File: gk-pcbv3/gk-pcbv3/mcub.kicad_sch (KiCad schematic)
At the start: 10 parts, among them U4 STM32H7S7L8H6H, Y1 24MHz

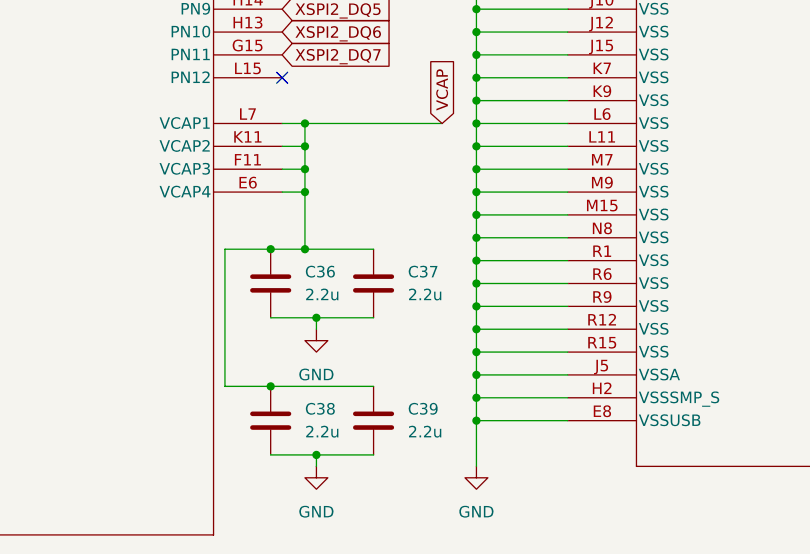
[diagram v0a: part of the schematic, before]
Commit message: redesign for better signal integrity
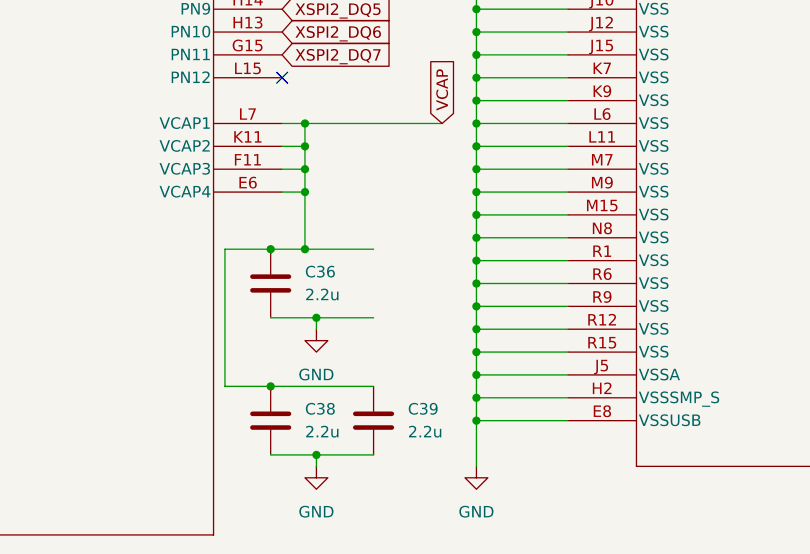
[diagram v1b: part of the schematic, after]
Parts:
- removed C37: 2.2u, Capacitor_SMD:C_0805_2012Metric, symbol Device:C
- C36, C38, C39: footprint Capacitor_SMD:C_0805_2012Metric -> Capacitor_SMD:C_0402_1005Metric
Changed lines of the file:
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@@
 			)
 		)
-		(property "Footprint" "Capacitor_SMD:C_0805_2012Metric"
+		(property "Footprint" "Capacitor_SMD:C_0402_1005Metric"
 			(at 133.0452 151.13 0)
 			(effects
@@
 	)
 	(symbol
-		(lib_id "Device:C")
-		(at 132.08 132.08 0)
-		(unit 1)
-		(exclude_from_sim no)
-		(in_bom yes)
-		(on_board yes)
-		(dnp no)
-		(fields_autoplaced yes)
-		(property "Reference" "C37"
-			(at 135.89 130.8099 0)
-			(effects
-				(font
-					(size 1.27 1.27)
-				)
-				(justify left)
-			)
-		)
-		(property "Value" "2.2u"
-			(at 135.89 133.3499 0)
-			(effects
-				(font
-					(size 1.27 1.27)
-				)
-				(justify left)
-			)
-		)
-		(property "Footprint" "Capacitor_SMD:C_0805_2012Metric"
-			(at 133.0452 135.89 0)
-			(effects
-				(font
-					(size 1.27 1.27)
-				)
-				(hide yes)
-			)
-		)
-		(property "Datasheet" "~"
-			(at 132.08 132.08 0)
-			(effects
-				(font
-					(size 1.27 1.27)
-				)
-				(hide yes)
-			)
-		)
-		(property "Description" "Unpolarized capacitor"
-			(at 132.08 132.08 0)
-			(effects
-				(font
-					(size 1.27 1.27)
-				)
-				(hide yes)
-			)
-		)
-		(pin "1"
-		)
-		(pin "2"
-		)
-		(instances
-			(project "gk-pcbv3"
-				(path "/08730ac6-6084-459f-bdf1-86b322355ede/ac32e8dc-0b6c-41cd-b88e-0eb0784dc95b"
-					(reference "C37")
-					(unit 1)
-				)
-			)
-		)
-	)
-	(symbol
 		(lib_id "power:VCC")
 		(at 222.25 128.27 90)
@@
 			)
 		)
-		(property "Footprint" "Capacitor_SMD:C_0805_2012Metric"
+		(property "Footprint" "Capacitor_SMD:C_0402_1005Metric"
 			(at 121.6152 151.13 0)
 			(effects
@@
 			)
 		)
-		(property "Footprint" "Capacitor_SMD:C_0805_2012Metric"
+		(property "Footprint" "Capacitor_SMD:C_0402_1005Metric"
 			(at 121.6152 135.89 0)
 			(effects
